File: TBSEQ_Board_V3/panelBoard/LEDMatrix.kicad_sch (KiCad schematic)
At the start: 32 parts

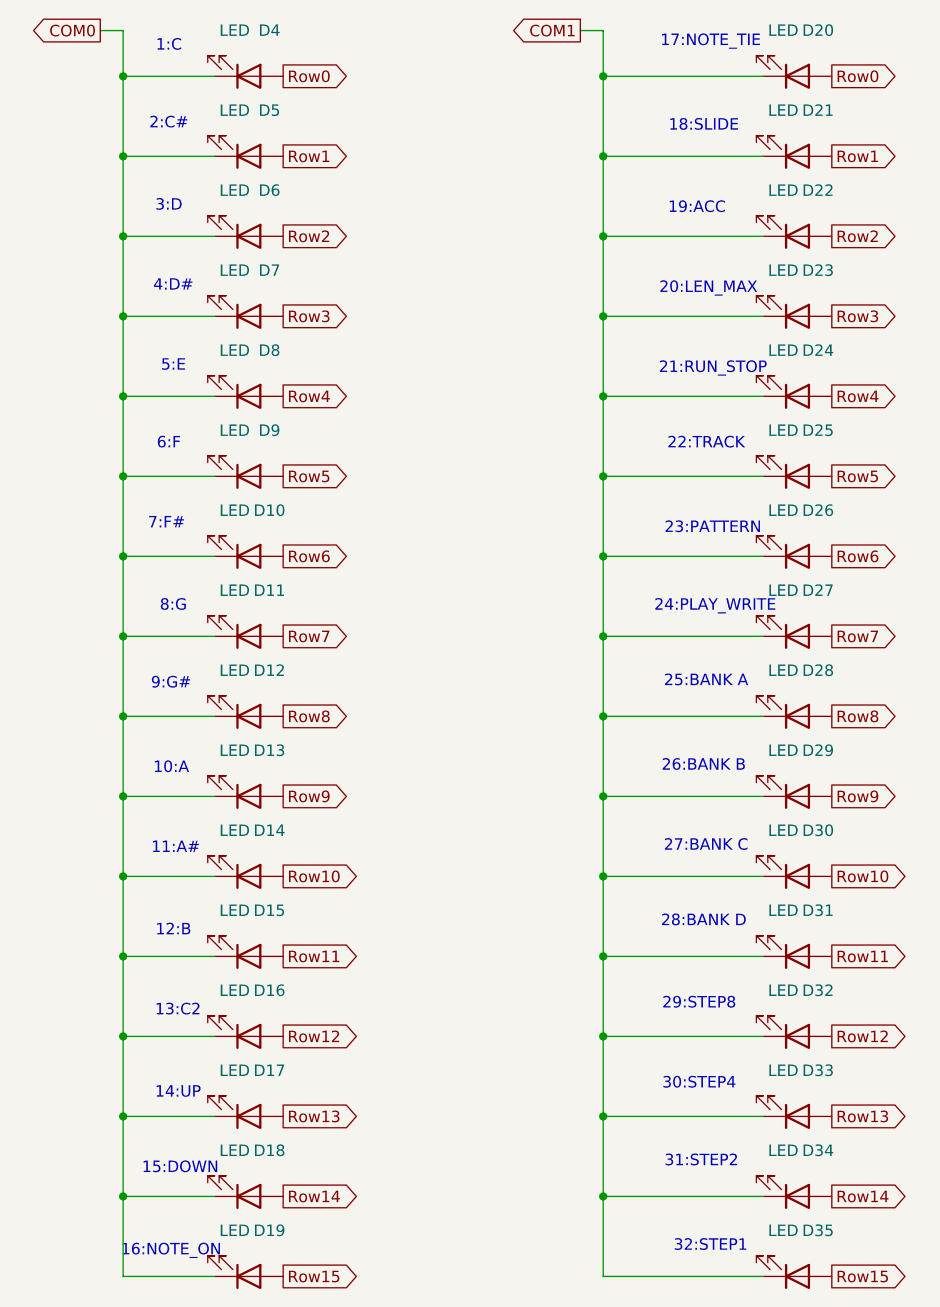
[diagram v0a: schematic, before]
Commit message: V3Board
PanelBoard⇒debugPanelBoardにして部品を全部表に出してアートワーク修正中
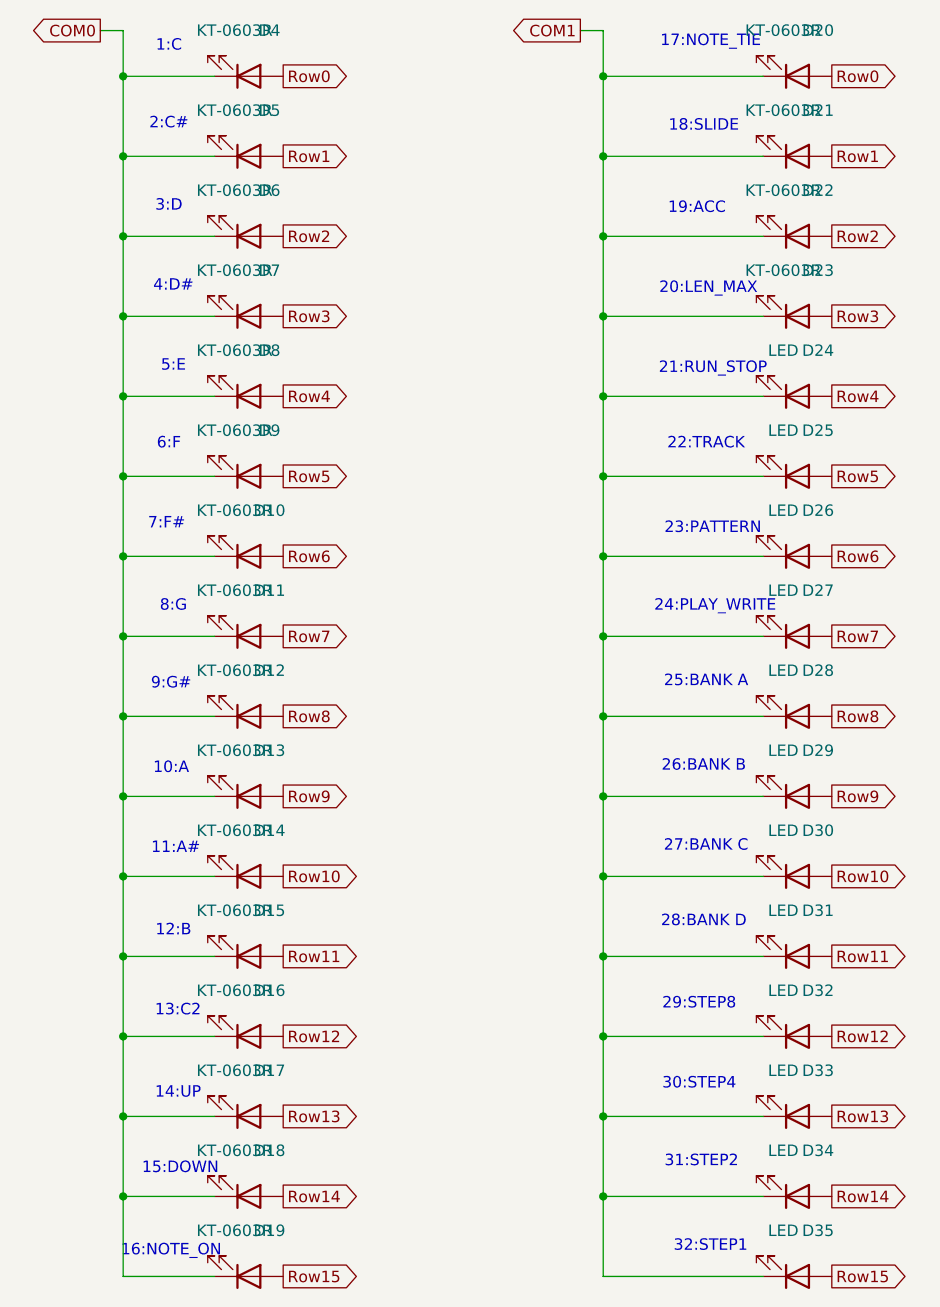
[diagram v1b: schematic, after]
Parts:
- D10, D11, D12, D13, D14, D15, D16, D17, D18, D19, D20, D21, D22, D23, D4, D5, D6, D7, D8, D9: value LED -> KT-0603R
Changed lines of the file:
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@@
 			)
 		)
-		(property "Value" "LED"
+		(property "Value" "KT-0603R"
 			(at 78.4225 134.62 0)
 			(effects
@@
 			)
 		)
-		(property "Value" "LED"
+		(property "Value" "KT-0603R"
 			(at 78.4225 161.29 0)
 			(effects
@@
 			)
 		)
-		(property "Value" "LED"
+		(property "Value" "KT-0603R"
 			(at 78.4225 152.4 0)
 			(effects
@@
 			)
 		)
-		(property "Value" "LED"
+		(property "Value" "KT-0603R"
 			(at 78.4225 107.95 0)
 			(effects
@@
 			)
 		)
-		(property "Value" "LED"
+		(property "Value" "KT-0603R"
 			(at 139.3825 54.61 0)
 			(effects
@@
 			)
 		)
-		(property "Value" "LED"
+		(property "Value" "KT-0603R"
 			(at 78.4225 99.06 0)
 			(effects
@@
 			)
 		)
-		(property "Value" "LED"
+		(property "Value" "KT-0603R"
 			(at 78.4225 36.83 0)
 			(effects
@@
 			)
 		)
-		(property "Value" "LED"
+		(property "Value" "KT-0603R"
 			(at 78.4225 63.5 0)
 			(effects
@@
 			)
 		)
-		(property "Value" "LED"
+		(property "Value" "KT-0603R"
 			(at 78.4225 90.17 0)
 			(effects
@@
 			)
 		)
-		(property "Value" "LED"
+		(property "Value" "KT-0603R"
 			(at 78.4225 81.28 0)
 			(effects
@@
 			)
 		)
-		(property "Value" "LED"
+		(property "Value" "KT-0603R"
 			(at 139.3825 45.72 0)
 			(effects
@@
 			)
 		)
-		(property "Value" "LED"
+		(property "Value" "KT-0603R"
 			(at 78.4225 143.51 0)
 			(effects
@@
 			)
 		)
-		(property "Value" "LED"
+		(property "Value" "KT-0603R"
 			(at 78.4225 27.94 0)
 			(effects
@@
 			)
 		)
-		(property "Value" "LED"
+		(property "Value" "KT-0603R"
 			(at 78.4225 54.61 0)
 			(effects
@@
 			)
 		)
-		(property "Value" "LED"
+		(property "Value" "KT-0603R"
 			(at 78.4225 125.73 0)
 			(effects
@@
 			)
 		)
-		(property "Value" "LED"
+		(property "Value" "KT-0603R"
 			(at 78.4225 116.84 0)
 			(effects
@@
 			)
 		)
-		(property "Value" "LED"
+		(property "Value" "KT-0603R"
 			(at 78.4225 45.72 0)
 			(effects
@@
 			)
 		)
-		(property "Value" "LED"
+		(property "Value" "KT-0603R"
 			(at 139.3825 36.83 0)
 			(effects
@@
 			)
 		)
-		(property "Value" "LED"
+		(property "Value" "KT-0603R"
 			(at 139.3825 27.94 0)
 			(effects
@@
 			)
 		)
-		(property "Value" "LED"
+		(property "Value" "KT-0603R"
 			(at 78.4225 72.39 0)
 			(effects
